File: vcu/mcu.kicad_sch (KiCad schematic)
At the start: 6 parts, among them J10 ZIO_CN10, J7 ZIO_CN8, J8 ZIO_CN9, J9 ZIO_CN7

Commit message: VCU changes - layout mostly done
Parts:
- removed J10: ZIO_CN10, Connector_PinSocket_2.54mm:PinSocket_2x17_P2.54mm_Vertical, symbol Connector_Generic:Conn_02x17_Odd_Even
- removed J7: ZIO_CN8, Connector_PinSocket_2.54mm:PinSocket_2x08_P2.54mm_Vertical, symbol Connector_Generic:Conn_02x08_Odd_Even
- removed J8: ZIO_CN9, Connector_PinSocket_2.54mm:PinSocket_2x15_P2.54mm_Vertical, symbol Connector_Generic:Conn_02x15_Odd_Even
- removed J9: ZIO_CN7, Connector_PinSocket_2.54mm:PinSocket_2x10_P2.54mm_Vertical, symbol Connector_Generic:Conn_02x10_Odd_Even
- added C13, C14, C15, C16, C17, C18, C19, C20, C21, C22, C23, C27, C29, C32, C33: 100n, Capacitor_SMD:C_0805_2012Metric_Pad1.18x1.45mm_HandSolder, symbol Device:C
- added C24: 4.7u, Capacitor_SMD:C_0805_2012Metric_Pad1.18x1.45mm_HandSolder, symbol Device:C
- added C25: 1u, Capacitor_SMD:C_0805_2012Metric_Pad1.18x1.45mm_HandSolder, symbol Device:C
- added C26, C28: 2.2u, Capacitor_SMD:C_0805_2012Metric_Pad1.18x1.45mm_HandSolder, symbol Device:C
- added C30, C31: 4.3p, Capacitor_SMD:C_0805_2012Metric_Pad1.18x1.45mm_HandSolder, symbol Device:C
- added C34: 10u, Capacitor_SMD:C_0805_2012Metric_Pad1.18x1.45mm_HandSolder, symbol Device:C
- added D2: LED, LED_SMD:LED_0805_2012Metric_Pad1.15x1.40mm_HandSolder, symbol Device:LED
- added FB1: 120, Resistor_SMD:R_0805_2012Metric_Pad1.20x1.40mm_HandSolder, symbol Device:FerriteBead
- added J8: Conn_ARM_JTAG_SWD_20, Connector_IDC:IDC-Header_2x10_P2.54mm_Vertical, symbol Connector:Conn_ARM_JTAG_SWD_20
- added R10: 10k, Resistor_SMD:R_0805_2012Metric_Pad1.20x1.40mm_HandSolder, symbol Device:R
- added R11, R13, R58, R59: 10k, Resistor_SMD:R_0805_2012Metric_Pad1.20x1.40mm_HandSolder, symbol Device:R_Small
- added R12: 1k5, Resistor_SMD:R_0805_2012Metric_Pad1.20x1.40mm_HandSolder, symbol Device:R
- added SW1: SW_SPDT, Button_Switch_THT:SW_Slide_1P2T_CK_OS102011MS2Q, symbol Switch:SW_SPDT
- added SW2: SW_Push, Button_Switch_THT:SW_PUSH_6mm, symbol Switch:SW_Push
- added U11: LD1117S33TR_SOT223, Package_TO_SOT_SMD:SOT-223-3_TabPin2, symbol Regulator_Linear:LD1117S33TR_SOT223
- added U9: STM32F746ZGT6, Package_QFP:LQFP-144_20x20mm_P0.5mm, symbol MCU_ST_STM32F7:STM32F746ZGTx
- added Y1: 8MHz, Crystal:Crystal_SMD_7050-2Pin_7.0x5.0mm_HandSoldering, symbol Device:Crystal
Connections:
- net APPS_1: now also U9.37 (PA3)
- net APPS_2: now also U9.29 (PC3)
- net BPS: now also U9.26 (PC0)
- net BRAKE_PRESSED: now also U9.64 (PE11)
- net CAN1_RX: now also U9.114 (PD0)
- net CAN1_TX: now also U9.115 (PD1)
- net CAN2_RX: now also U9.73 (PB12)
- net CAN2_TX: now also U9.136 (PB6)
- net DRS: now also U9.34 (PA0)
- net DRS_BTN: now also U9.22 (PF10)
- net DRS_LED: now also U9.3 (PE4)
- net EEPROM_WC: now also U9.96 (PC6)
- net GND: now also R48.1, C13.2, C14.2, C15.2, C16.2, C17.2, C18.2, C19.2, C20.2, C21.2, C22.2, C23.2, C24.2, C25.2, C26.1, C27.2, C28.1, C29.2, C30.2, C31.2, C32.2, C33.2, C34.2, J8.10 (GND), J8.11 (RTCK), J8.12 (GND), J8.14 (GND), J8.16 (GND), J8.18 (GND), J8.20 (GND), J8.4 (GND), J8.6 (GND), J8.8 (GND), R12.2, SW1.1 (A), SW2.1, U11.1 (GND), U9.107 (VSS), U9.120 (VSS), U9.130 (VSS), U9.16 (VSS), U9.31 (VSSA), U9.38 (VSS), U9.51 (VSS), U9.61 (VSS), U9.83 (VSS), U9.94 (VSS)
- net R2D_BTN: now also U9.12 (PF2)
- net R2D_LED: now also U9.5 (PE6)
- net R2D_SIREN: now also U9.55 (PF15)
- net SAGL: now also U9.13 (PF3)
- net SCL: now also R58.2, U9.139 (PB8); no longer R49.2
- net SDA: now also R13.1, U9.140 (PB9); no longer R48.1
- net SHDN: now also U9.11 (PF1)
- net STATUS: now also U9.60 (PE9)
- net TS_ON: now also U9.54 (PF14)
- net TS_ON_BTN: now also U9.15 (PF5)
- net TS_ON_LED: now also U9.4 (PE5)
- net VC_LEDS: now also U9.2 (PE3)
- net VIN: now also C33.1, U11.3 (VI)
- net +3V3 renamed TCK/SWDCLK
- net TCK/SWDCLK: now also J8.9 (TCK/SWDCLK), U9.109 (PA14); no longer R49.1
- new net: C28.2, U9.106 (VCAP_2)
- new net: C26.2, U9.71 (VCAP_1)
- new net: C31.1, U9.24 (PH1), Y1.2
- new net: C30.1, U9.23 (PH0), Y1.1
- new net +3.3V: C13.1, C14.1, C15.1, C16.1, C17.1, C18.1, C19.1, C20.1, C21.1, C22.1, C23.1, C24.1, C25.1, C32.1, C34.1, D2.2 (A), FB1.2, J8.1 (VTREF), J8.2 (VCC/NC), R11.2, R13.2, R49.2, R58.1, R59.2, SW1.3 (C), U11.2 (VO), U9.108 (VDD), U9.121 (VDD), U9.131 (VDD), U9.144 (VDD), U9.17 (VDD), U9.30 (VDD), U9.39 (VDD), U9.52 (VDD), U9.6 (VBAT), U9.62 (VDD), U9.72 (VDD), U9.84 (VDD), U9.95 (VDDUSB)
- new net +3.3VA: C27.1, FB1.1, U9.32 (VREF+), U9.33 (VDDA)
- new net BOOT0: R10.2, U9.138 (BOOT0)
- new net NRST: C29.1, J8.15 (~{SRST}), SW2.2, U9.25 (NRST)
- new net PWR_LED_K: D2.1 (K), R12.1
- new net SW_BOOT0: R10.1, SW1.2 (B)
- new net TDI: J8.5 (TDI), R49.1, U9.110 (PA15)
- new net TDO/SWO: J8.13 (TDO/SWO), U9.133 (PB3)
- new net TMS/SWDIO: J8.7 (TMS/SWDIO), R59.1, U9.105 (PA13)
- new net TRST: J8.3 (~{TRST}), R11.1, U9.134 (PB4)
- no-connect marks 66 -> 86
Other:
- note added: "12V -> 3.3V"
- note added: "800mA Maximum"
- note added: "ARM 20-Pin JTAG(5-bits)/Serial Wire Debugger"
- note added: "Analog Voltage Filter"
- note added: "Decoupling Capacitors"
- note added: "Linear Voltage Regulator"
- note added: "STM32F746ZGT6"
- note removed: "+3V3"
- note removed: "+5V"
- note removed: "AGND"
- note removed: "AVDD"
- note removed: "GND"
- note removed: "IOREF"
- note removed: "NC"
- note removed: "Nucleo-144 dev board has built in LD1117 regulator supplied from VIN which provides 3.3V power for rest of circuit, up to 800mA"
- note removed: "PA0"
- note removed: "PA15"
- note removed: "PA3"
- note removed: "PA4"
- note removed: "PA5"
- note removed: "PA6"
- note removed: "PA7"
- note removed: "PB0"
- note removed: "PB1"
- note removed: "PB10"
- note removed: "PB11"
- note removed: "PB12"
- note removed: "PB13"
- note removed: "PB15"
- note removed: "PB2"
- note removed: "PB3"
- note removed: "PB4"
- note removed: "PB5"
- note removed: "PB6"
- note removed: "PB8"
- note removed: "PB9"
- note removed: "PC0"
- note removed: "PC10"
- note removed: "PC11"
- note removed: "PC12"
- note removed: "PC2"
- note removed: "PC3"
- note removed: "PC6"
- note removed: "PC7"
- note removed: "PC8"
- note removed: "PC9"
- note removed: "PD0"
- note removed: "PD1"
- note removed: "PD11"
- note removed: "PD12"
- note removed: "PD13"
- note removed: "PD14"
- note removed: "PD15"
- note removed: "PD2"
- note removed: "PD3"
- note removed: "PD4"
- note removed: "PD5"
- note removed: "PD6"
- note removed: "PD7"
- note removed: "PE0"
- note removed: "PE10"
- note removed: "PE11"
- note removed: "PE13"
- note removed: "PE14"
- note removed: "PE15"
- note removed: "PE2"
- note removed: "PE3"
- note removed: "PE4"
- note removed: "PE5"
- note removed: "PE6"
- note removed: "PE7"
- note removed: "PE8"
- note removed: "PE9"
- note removed: "PF0"
- note removed: "PF1"
- note removed: "PF10"
- note removed: "PF12"
- note removed: "PF13"
- note removed: "PF14"
- note removed: "PF15"
- note removed: "PF2"
- note removed: "PF3"
- note removed: "PF4"
- note removed: "PF5"
- note removed: "PF7"
- note removed: "PF8"
- note removed: "PF9"
- note removed: "PG0"
- note removed: "PG1"
- note removed: "PG14"
- note removed: "PG2"
- note removed: "PG3"
- note removed: "PG9"
- note removed: "RESET"
- note removed: "STM32 F746ZG Nucleo-144 Zio"
- note removed: "To set bus time constant (RC < 400ns)"
- note removed: "VIN"

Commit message: Changed crystal footprint to more appropriate and available size
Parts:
- Y1: footprint Crystal:Crystal_SMD_7050-2Pin_7.0x5.0mm_HandSoldering -> Crystal:Crystal_HC49-U_Vertical
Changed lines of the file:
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@@
       (effects (font (size 1.27 1.27)))
     )
-    (property "Footprint" "Crystal:Crystal_SMD_7050-2Pin_7.0x5.0mm_HandSoldering" (at 61.214 70.358 0)
+    (property "Footprint" "Crystal:Crystal_HC49-U_Vertical" (at 61.214 70.358 0)
       (effects (font (size 1.27 1.27)) hide)
     )

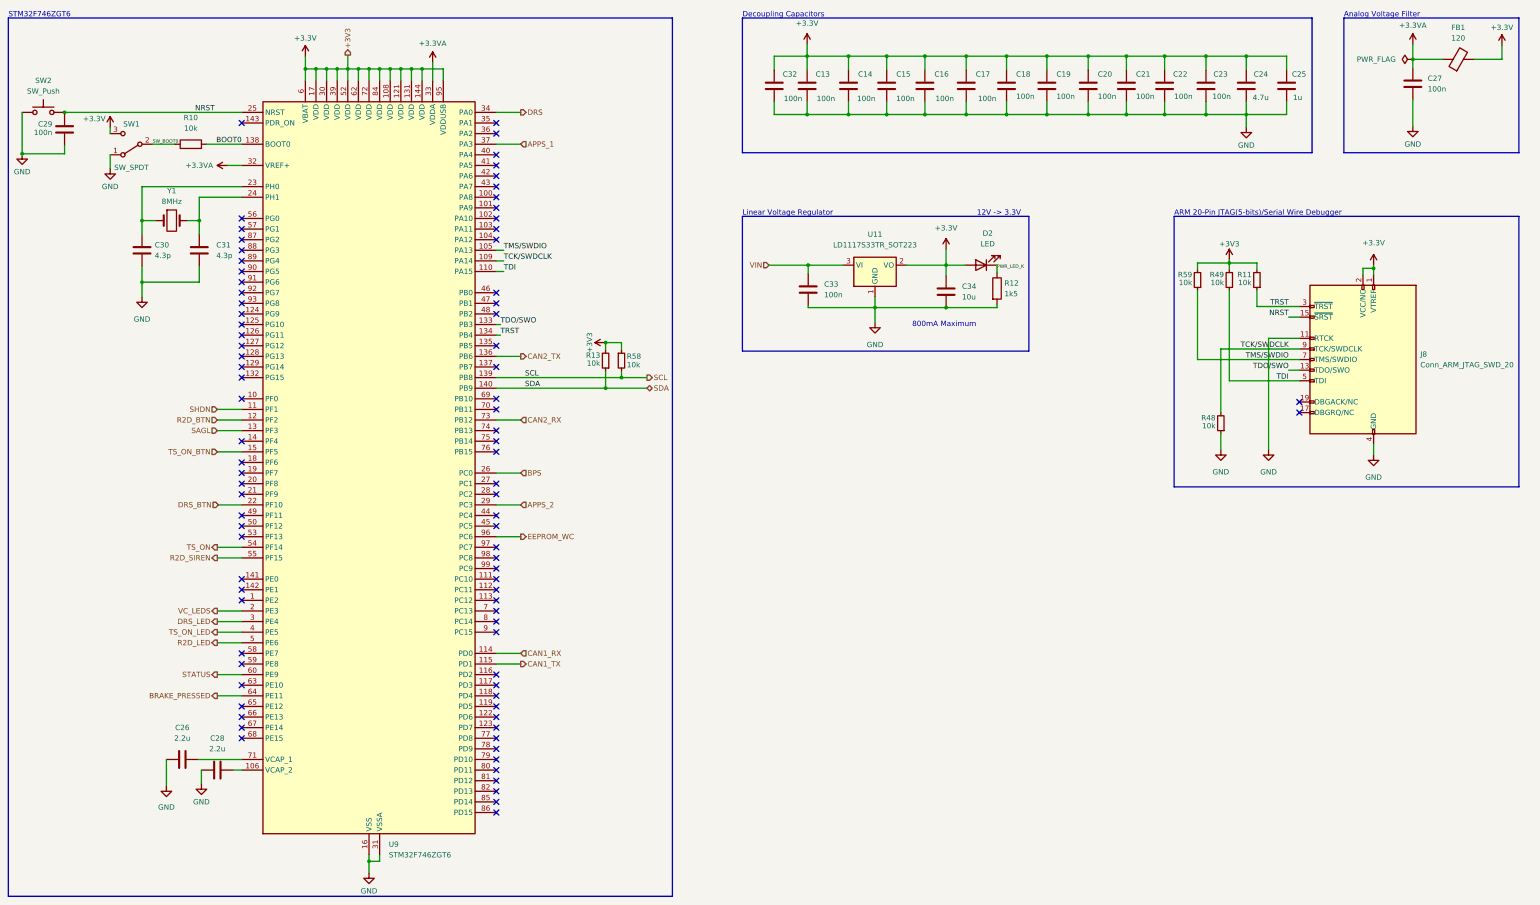
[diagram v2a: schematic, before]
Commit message: Added telemetry schematic and PCB to vcu project, made seperate power label for telemetry 3.3V
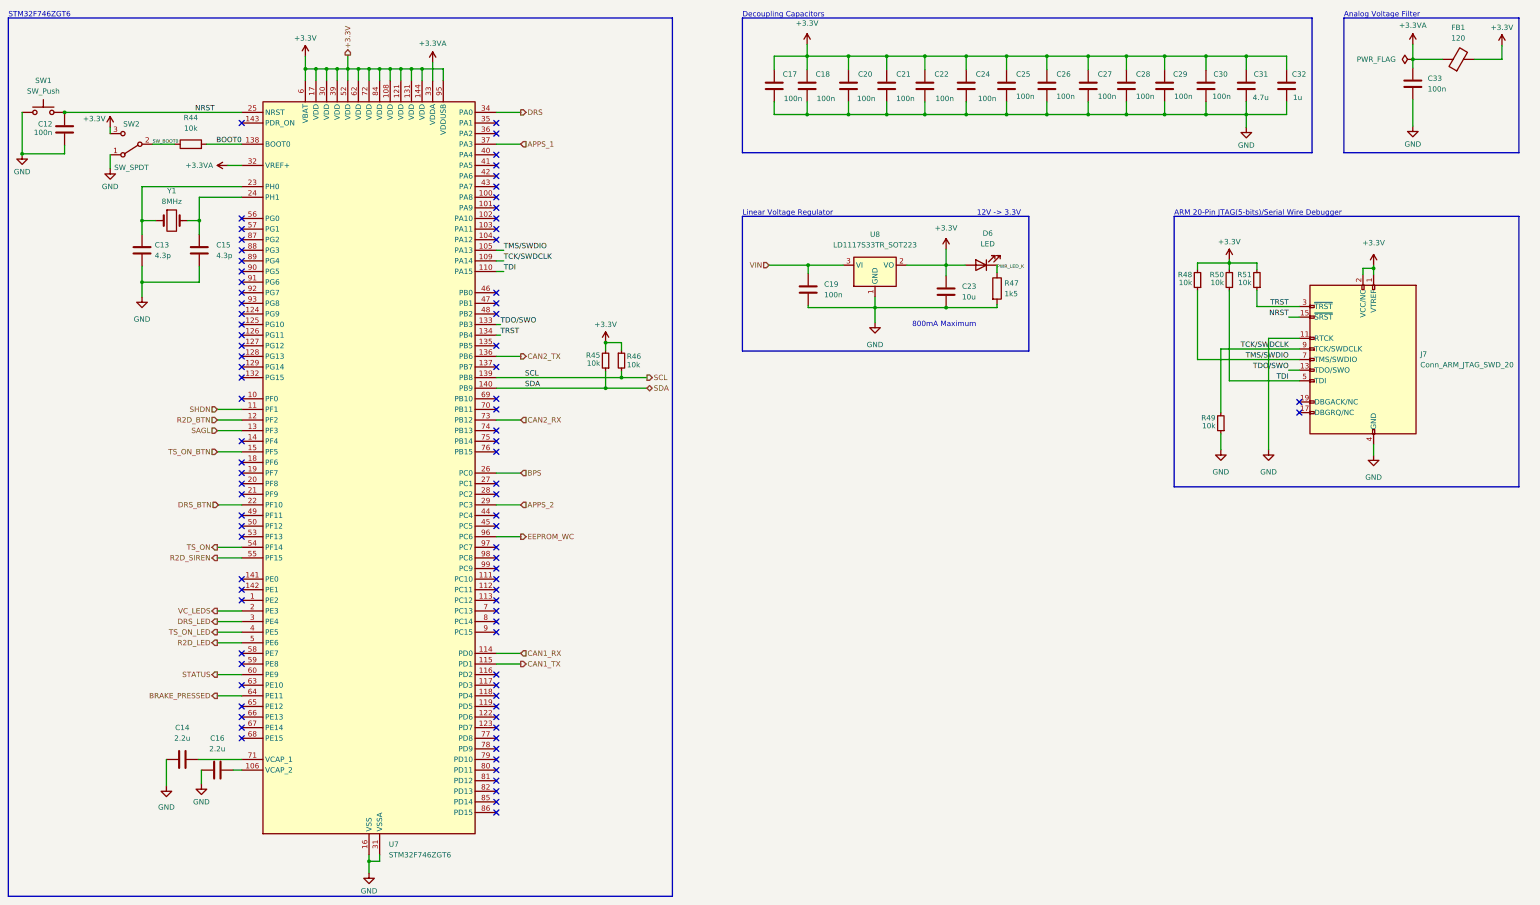
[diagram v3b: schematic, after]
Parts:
- renumbered C29 to C12, C30 to C13, C26 to C14, C31 to C15, C28 to C16, C32 to C17, C13 to C18, C33 to C19, C14 to C20, C15 to C21, C16 to C22, C34 to C23, C17 to C24, C18 to C25, C19 to C26, C20 to C27, C21 to C28, C22 to C29, C23 to C30, C24 to C31, C25 to C32, C27 to C33, D2 to D6, J8 to J7, R10 to R44, R13 to R45, R58 to R46, R12 to R47, R59 to R48, R48 to R49, R49 to R50, R11 to R51, SW2 to SW1, SW1 to SW2, U9 to U7, U11 to U8

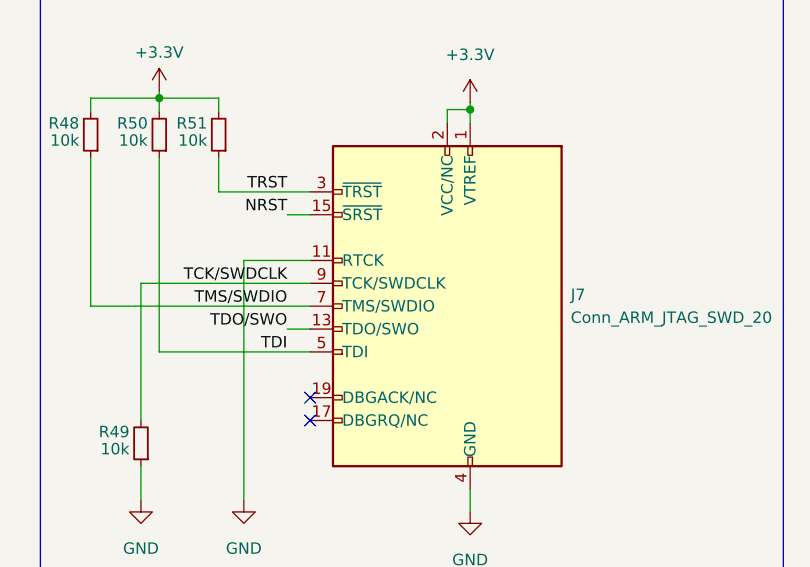
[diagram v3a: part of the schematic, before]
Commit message: Caps on analogue inputs, jumper on RTD resistor
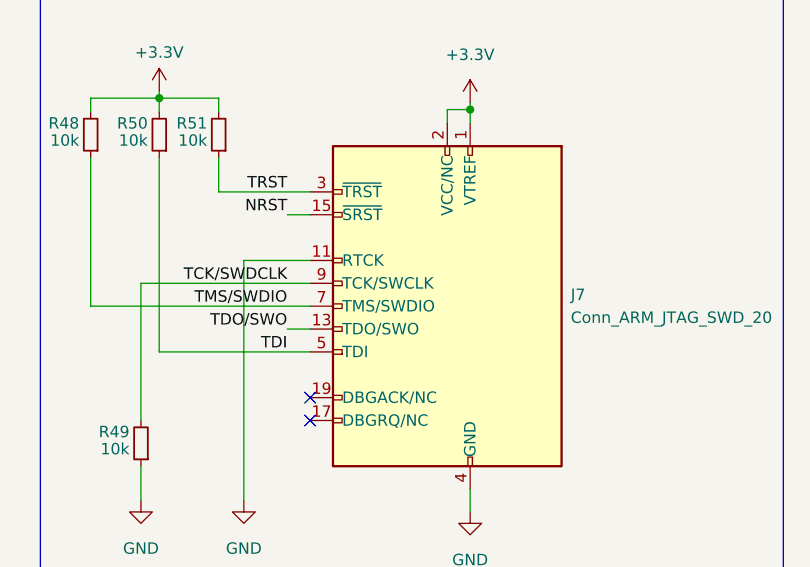
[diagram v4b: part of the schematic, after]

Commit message: Started making VCU changes
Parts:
- added J16: Spare pins, Connector_PinHeader_2.54mm:PinHeader_1x06_P2.54mm_Vertical, symbol Connector_Generic:Conn_01x06
- added R77, R78, R79, R80, R81, R82: 100, Resistor_SMD:R_0805_2012Metric_Pad1.20x1.40mm_HandSolder, symbol Device:R_Small
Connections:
- net at U7.100 (PA8): now also R79.1
- net at U7.101 (PA9): now also R80.1
- net at U7.102 (PA10): now also R81.1
- net at U7.103 (PA11): now also R82.1
- net at U7.42 (PA6): now also R77.1
- net at U7.43 (PA7): now also R78.1
- new net: J16.1 (Pin_1), R77.2
- new net: J16.2 (Pin_2), R78.2
- new net: J16.3 (Pin_3), R79.2
- new net: J16.4 (Pin_4), R80.2
- new net: J16.5 (Pin_5), R81.2
- new net: J16.6 (Pin_6), R82.2
- no-connect marks 86 -> 80
